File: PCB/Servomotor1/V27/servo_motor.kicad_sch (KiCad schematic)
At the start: 108 parts, among them J1 Serial Port, J2 Programming, J3 Screw_Terminal_01x03, J4 RS485, J5 Power IN, J6 Encoder, P1 Board_to_Board_Connector, P2 Board_to_Board_Connector, P3 Board_to_Board_Connector, P4 Board_to_Board_Connector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

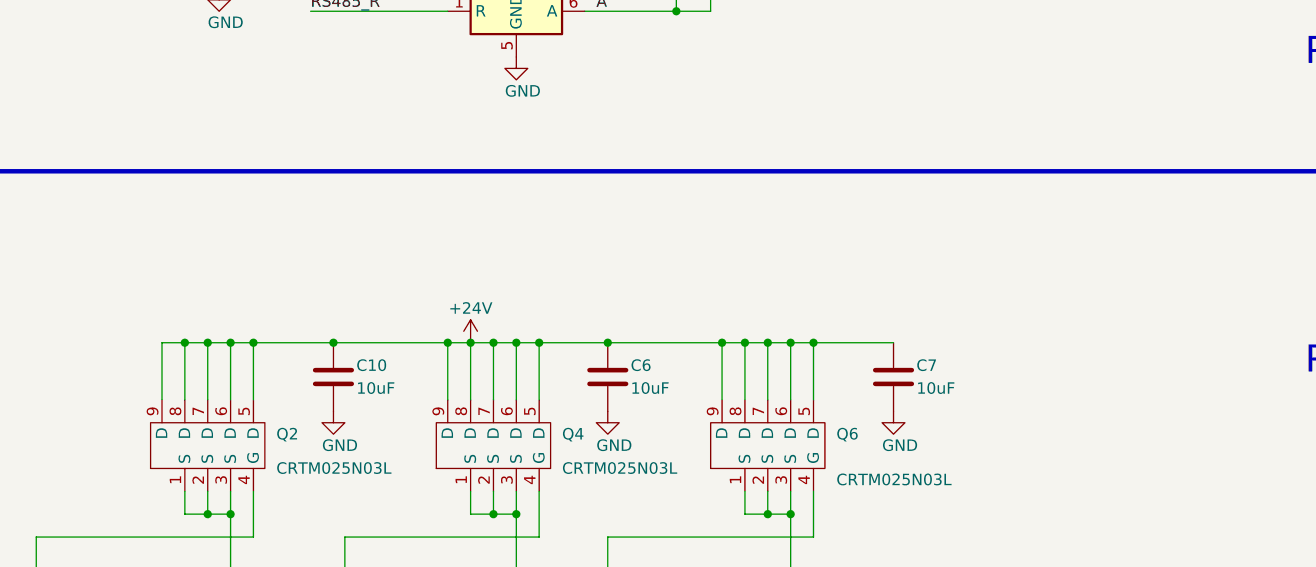
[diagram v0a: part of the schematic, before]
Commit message: Adding overtemperature protection and ability to read the temperature with a command Bug fixes and code improvements Added a few new tests to a new folfer called motor_tests
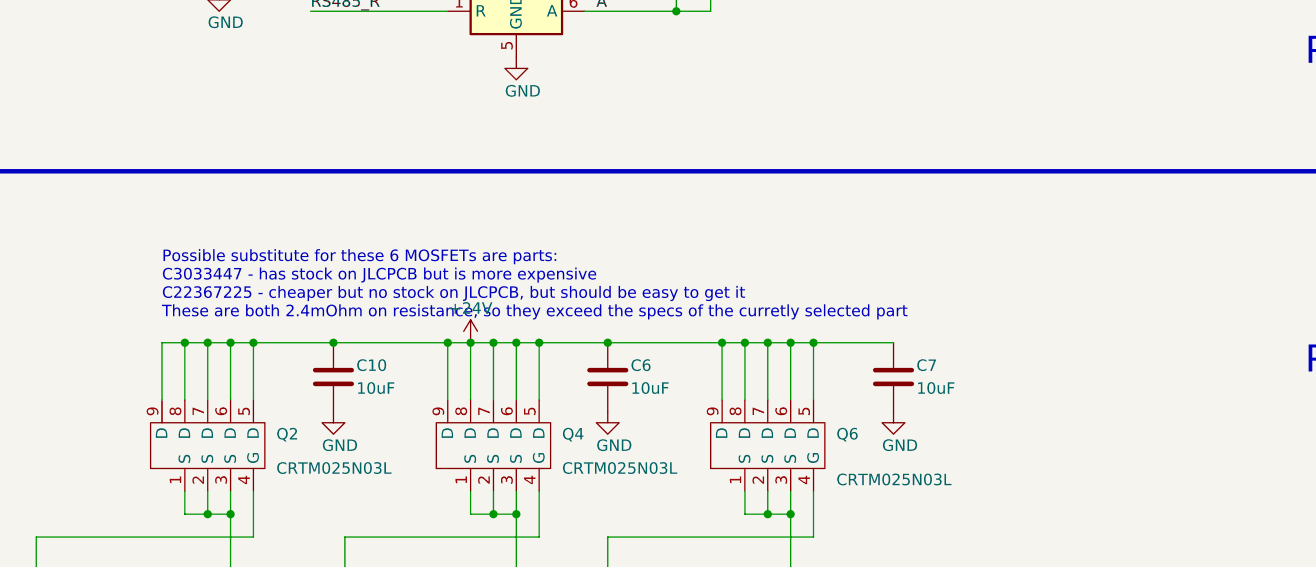
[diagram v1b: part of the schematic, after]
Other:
- note added: "Possible substitute for these 6 MOSFETs are parts: C3033447 - has stock on JLCPCB but is more expensive C22367225 - cheaper but no stock on JLCPCB, but should be easy to get it These are both 2.4mOhm on resistance, so they exceed the specs of the curretly selected part"
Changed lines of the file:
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@@
     (stroke (width 0) (type default))
+  )
+  (text "Possible substitute for these 6 MOSFETs are parts:\nC3033447 - has stock on JLCPCB but is more expensive\nC22367225 - cheaper but no stock on JLCPCB, but should be easy to get it\nThese are both 2.4mOhm on resistance, so they exceed the specs of the curretly selected part"
+    (at 152.4 154.94 0)
+    (effects (font (size 1.27 1.27)) (justify left bottom))
   )
   (text "Mar. 30, 2023" (at 330.2 280.67 0)
